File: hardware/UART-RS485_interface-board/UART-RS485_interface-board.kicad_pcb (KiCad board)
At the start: 4 copper layers, 68.6 x 27.9 mm, 15 parts, among them J1 UART (ESP32), J2 3V3, GND, J3 3V3, GND, J8 RS485 (Sensor), U2 MAX3485

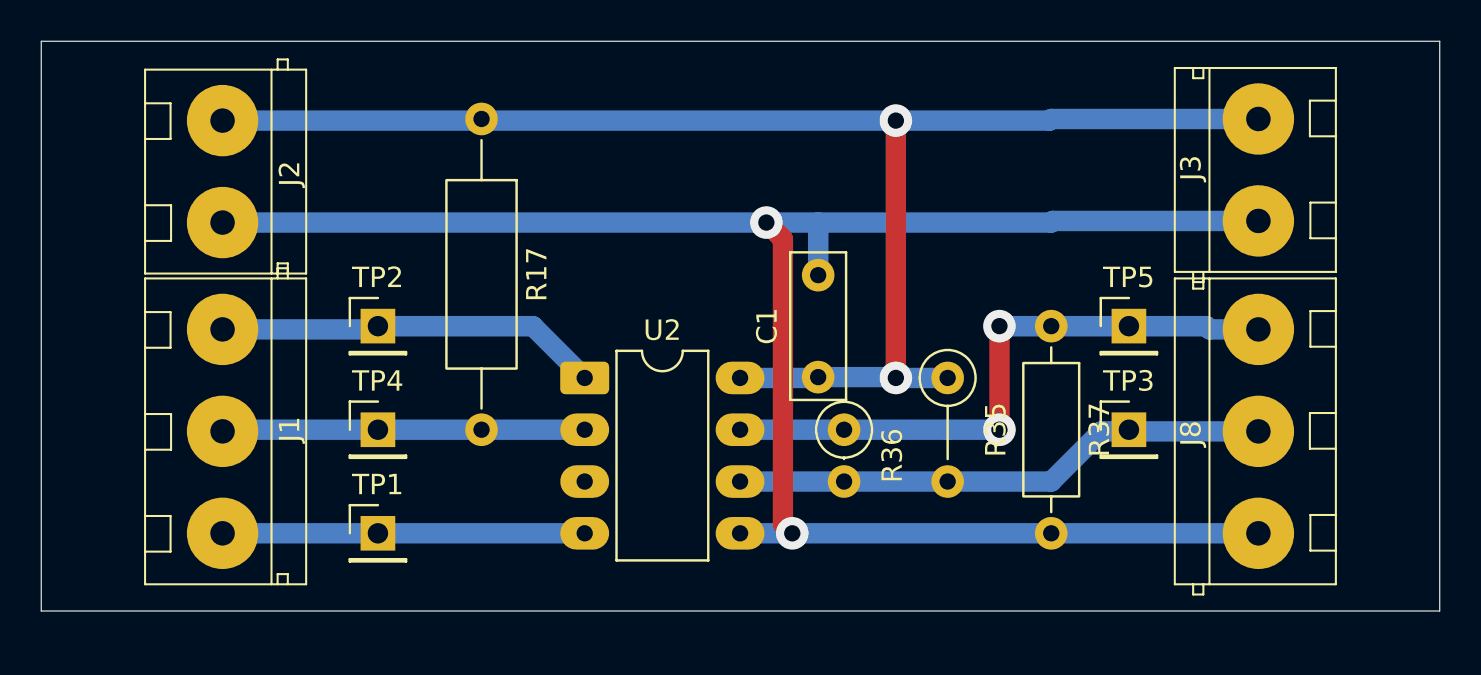
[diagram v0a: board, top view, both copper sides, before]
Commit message: UART-RS485 Stripboard: Adjust as actually soldered, fixes, add exports
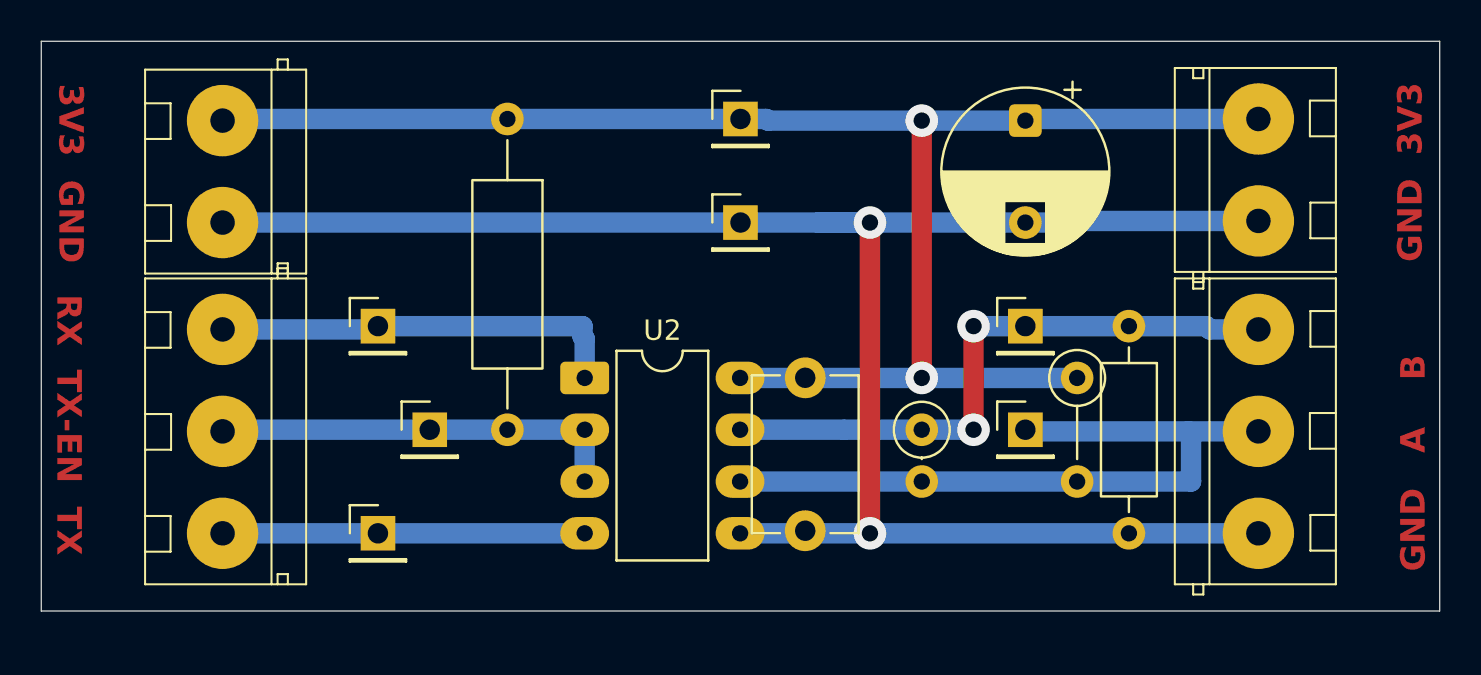
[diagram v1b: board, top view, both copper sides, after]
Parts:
- added C2: 10uf, Capacitor_THT:CP_Radial_D8.0mm_P5.00mm, F.Cu at (174.0, 45.8)
- added TP6: 3v3, Connector_PinHeader_2.54mm:PinHeader_1x01_P2.54mm_Vertical, F.Cu at (160.0, 45.7)
- added TP7: gnd, Connector_PinHeader_2.54mm:PinHeader_1x01_P2.54mm_Vertical, F.Cu at (160.0, 50.8)
- C1: footprint Capacitor_THT:C_Disc_D7.0mm_W2.5mm_P5.00mm -> Capacitor_THT:C_Disc_D7.5mm_W5.0mm_P7.50mm
- J1: value UART (ESP32) -> [TX, DIR, RX] UART (ESP32)
- J2, J3: value 3V3, GND -> GND, 3v3
- J8: value RS485 (Sensor) -> [GND, A, B] RS485 (Sensor)
- R35, R37: value 470 -> 3k3
- TP3: value TP A -> RS-A
- TP5: value TP B -> RS-B
- moved R35 6.35 mm to (176.5, 58.4)
- moved TP3 5.08 mm to (174.0, 61.0)
- moved TP5 5.08 mm to (174.0, 55.9)
- moved R36 3.81 mm to (168.9, 61.0)
- moved R37 3.81 mm to (179.1, 55.9)
- moved TP4 2.54 mm to (144.8, 61.0)
- moved R17 1.27 mm to (148.6, 45.7)
- moved C1 0.64 mm to (163.2, 58.4), turned to -90 degrees
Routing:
- net /RS485-A: track 26.3 -> 36.1 mm
- net +3V3: track 73.7 -> 80.1 mm
- net /RS485_DIR: track 17.8 -> 20.3 mm
- net GND: track 94.6 -> 96.6 mm
- net /RS485_RX: track 18.9 -> 20.3 mm
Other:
- board text added: "3V3 GND"
- board text added: "GND 3V3"
- board text added: "GND A B"
- board text added: "Mill / Isolate Strip"
- board text added: "Note: arranged as actually placed on the stripboard (overlaps)"
- board text added: "RX TX-EN TX"
- board text added: "Solder / Short Strips"
